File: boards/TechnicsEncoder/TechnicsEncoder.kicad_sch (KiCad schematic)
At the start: 20 parts, among them J1 ISP, J2 Bender, J3 Technics, J4 SelectRX, J5 MIDI In, J6 MIDI Out, J7 BoardCon, J8 PistonEncoder, U1 ATmega48-20P, U2 6N138

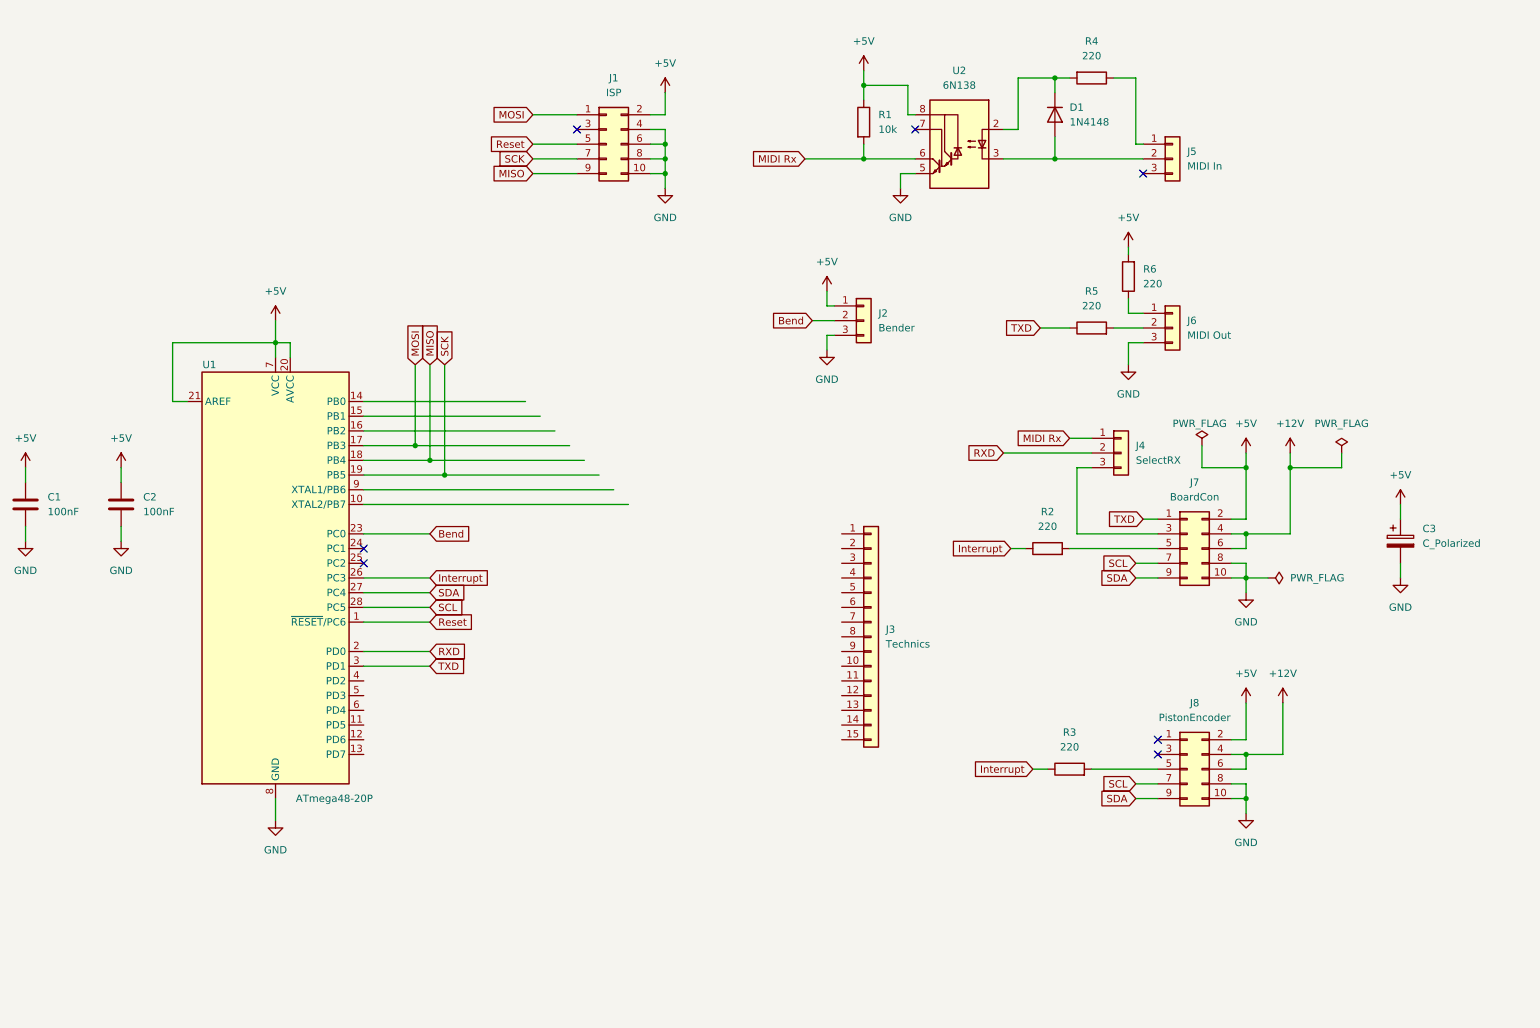
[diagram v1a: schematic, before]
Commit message: Added output buffer to MIDI outputs
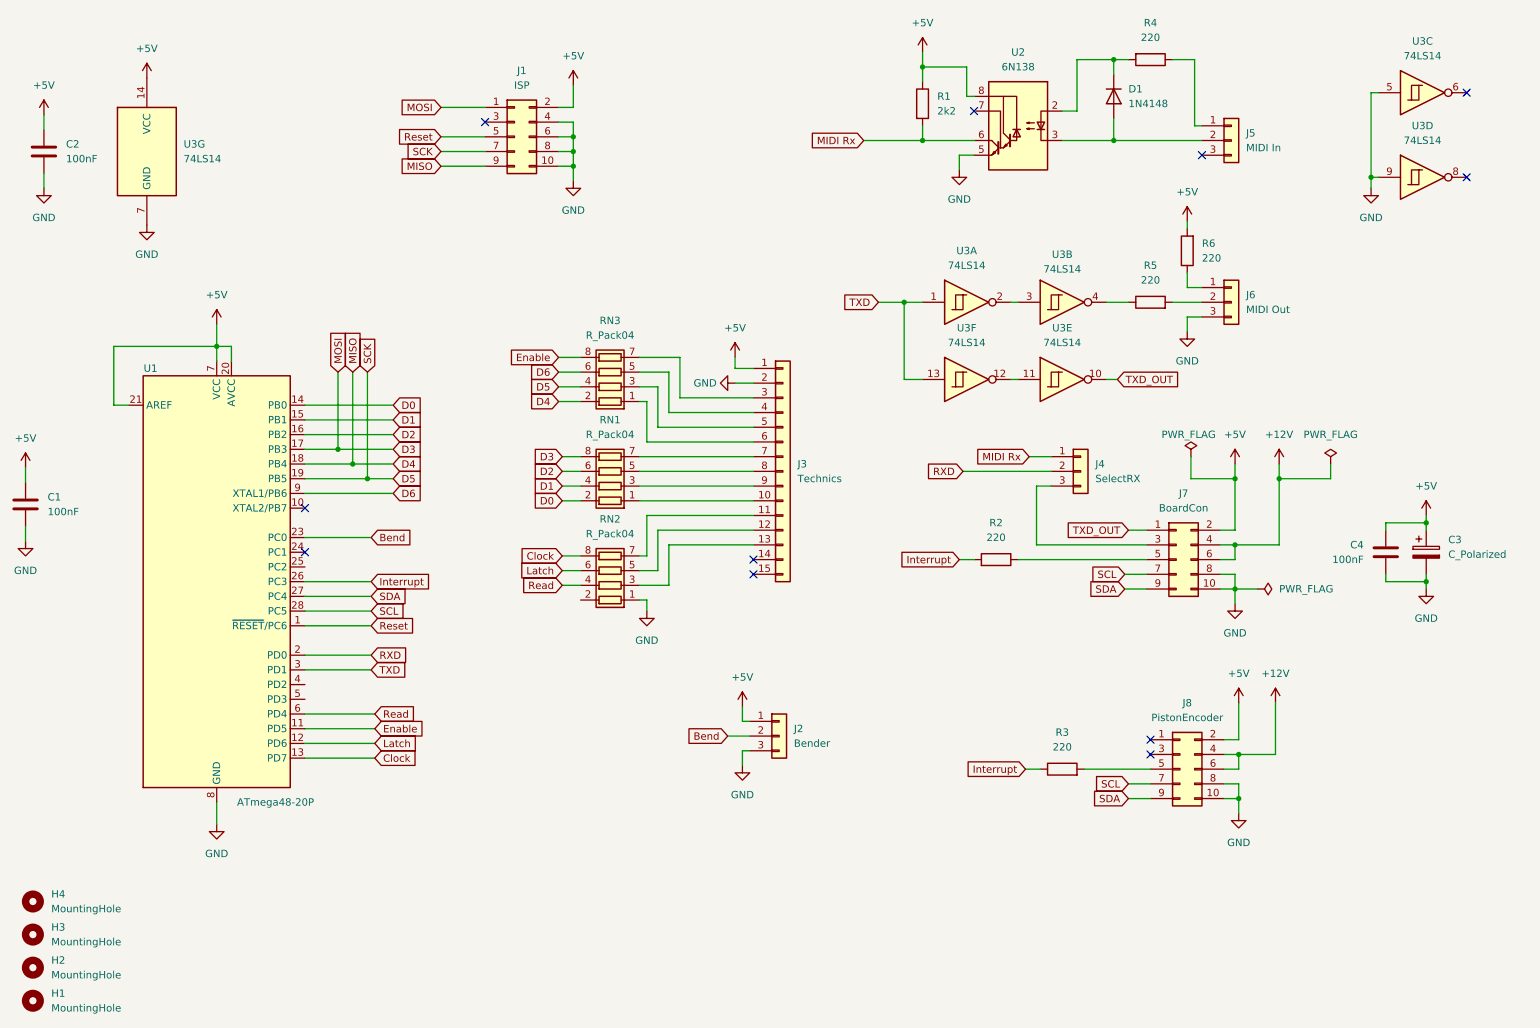
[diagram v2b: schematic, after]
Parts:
- added C4: 100nF, symbol Device:C
- added H1, H2, H3, H4: MountingHole, MountingHole:MountingHole_3mm, symbol Mechanical:MountingHole
- added RN1, RN2, RN3: R_Pack04, symbol Resistors_SIL:R_Pack04_SIL
- added U3: 74LS14, symbol 74xx:74LS14
- R1: value 10k -> 2k2
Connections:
- net +5V: now also J3.1 (Pin_1), C4.1, U3.14 (VCC)
- net GND: now also J3.2 (Pin_2), C4.2, RN2.1 (R1.1), U3.5, U3.7 (GND), U3.9
- net Interrupt: now also R2.2; no longer R2.1
- net TXD: now also U3.1, U3.13; no longer J7.1 (Pin_1), R5.1
- net at J3.10 (Pin_10): now also RN1.1 (R1.1)
- net at J3.11 (Pin_11): now also RN2.7 (R4.1)
- net at J3.12 (Pin_12): now also RN2.5 (R3.1)
- net at J3.13 (Pin_13): now also RN2.3 (R2.1)
- net at J3.3 (Pin_3): now also RN3.7 (R4.1)
- net at J3.4 (Pin_4): now also RN3.5 (R3.1)
- net at J3.5 (Pin_5): now also RN3.3 (R2.1)
- net at J3.6 (Pin_6): now also RN3.1 (R1.1)
- net at J3.7 (Pin_7): now also RN1.7 (R4.1)
- net at J3.8 (Pin_8): now also RN1.5 (R3.1)
- net at J3.9 (Pin_9): now also RN1.3 (R2.1)
- net at J7.5 (Pin_5): now also R2.1; no longer R2.2
- net Enable: now reaches U1.11 (PD5)
- net Enable: now also RN3.8 (R4.2)
- net Latch: now reaches U1.12 (PD6)
- net Latch: now also RN2.6 (R3.2)
- net Clock: now reaches U1.13 (PD7)
- net Clock: now also RN2.8 (R4.2)
- net D0: now reaches U1.14 (PB0)
- net D0: now also RN1.2 (R1.2)
- net D1: now reaches U1.15 (PB1)
- net D1: now also RN1.4 (R2.2)
- net D2: now reaches U1.16 (PB2)
- net D2: now also RN1.6 (R3.2)
- net Read: now reaches U1.6 (PD4)
- net Read: now also RN2.4 (R2.2)
- net D6: now reaches U1.9 (XTAL1/PB6)
- net D6: now also RN3.6 (R3.2)
- net MISO renamed D4
- net D4: now also RN3.2 (R1.2)
- net MOSI renamed D3
- net D3: now also RN1.8 (R4.2)
- net SCK renamed D5
- net D5: now also RN3.4 (R2.2)
- new net: U3.2, U3.3
- new net: R5.1, U3.4
- new net: U3.11, U3.12
- new net TXD_OUT: J7.1 (Pin_1), U3.10
- no-connect marks 7 -> 11
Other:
- moved on the sheet: C2, C3, D1, J1, J2, J3, J4, J5, J6, J7, J8, R1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

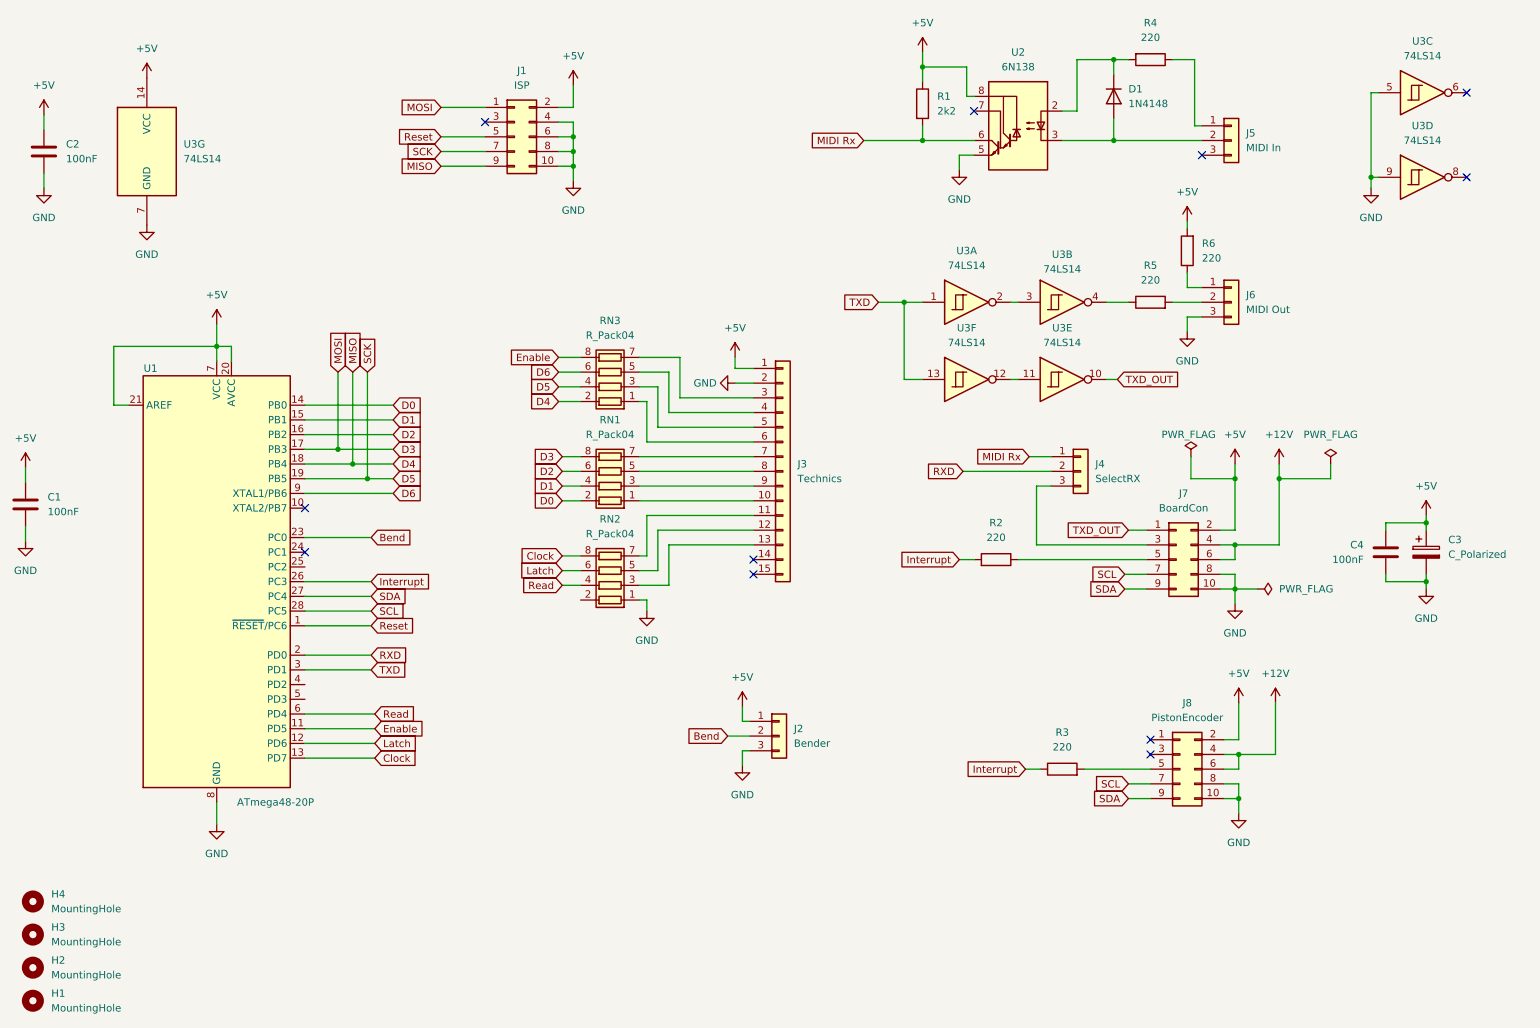
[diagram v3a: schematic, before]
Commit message: Using custom TO220 cooler, fixed and finished several PCBs
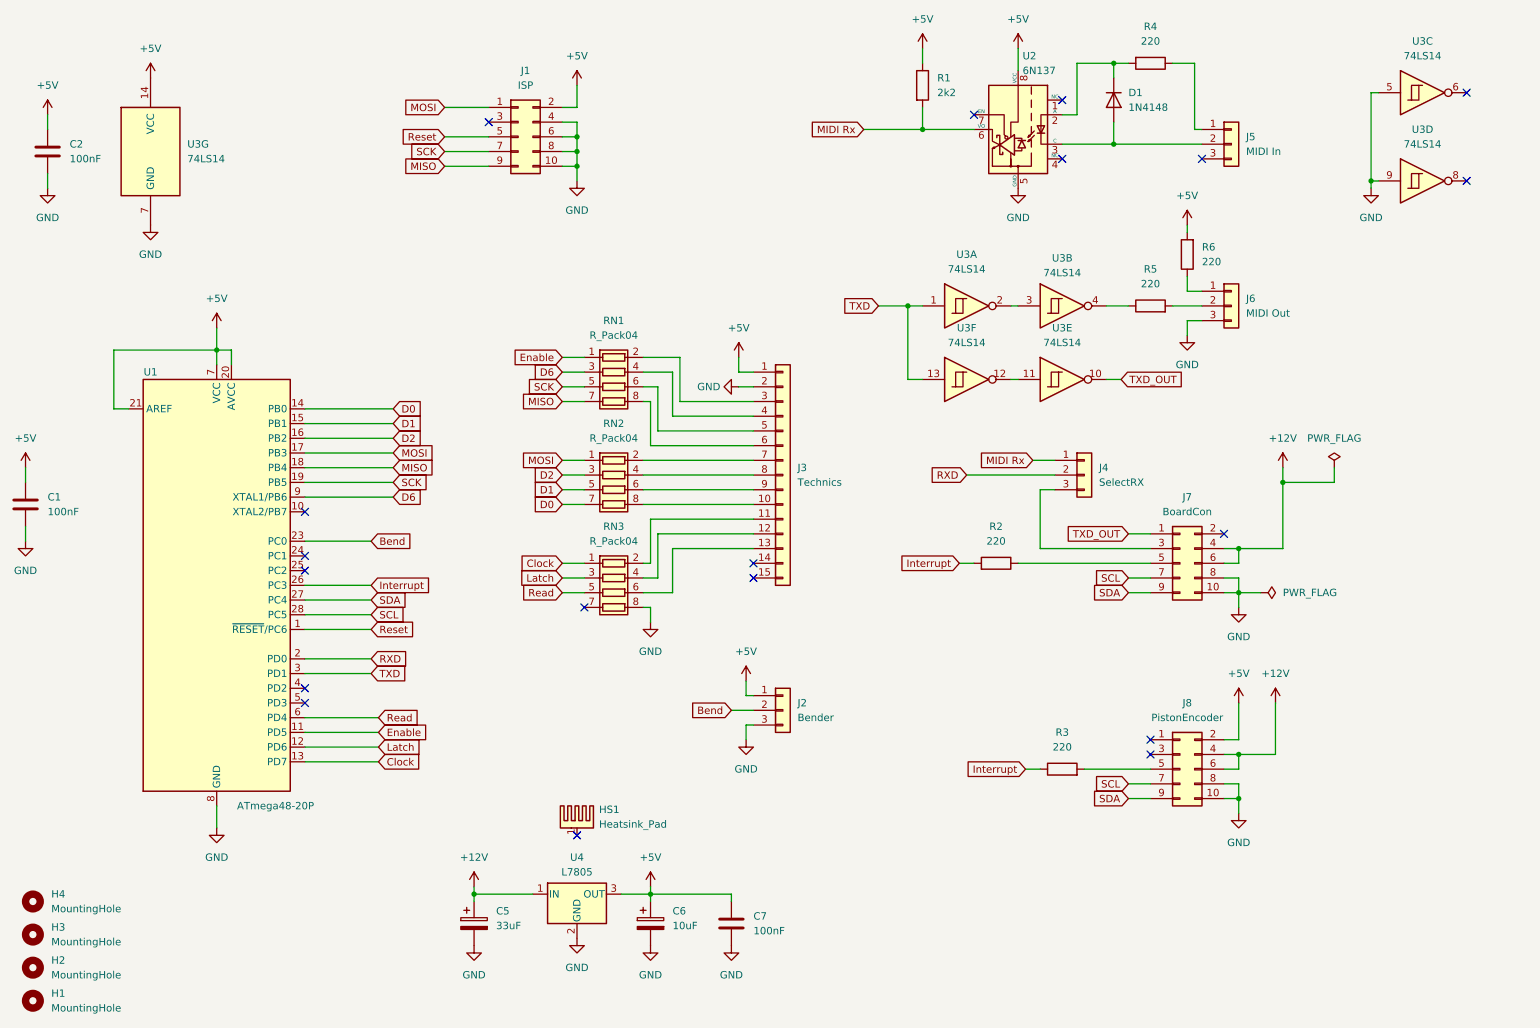
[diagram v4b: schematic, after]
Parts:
- removed C3: C_Polarized, symbol Device:C_Polarized
- removed C4: 100nF, symbol Device:C
- removed RN1, RN2, RN3: R_Pack04, symbol Resistors_SIL:R_Pack04_SIL
- removed U2: 6N138, Package_DIP:DIP-8_W7.62mm, symbol Isolator:6N138
- added C5: 33uF, Capacitor_THT:CP_Radial_D7.5mm_P2.50mm, symbol Device:C_Polarized
- added C6: 10uF, Capacitor_THT:CP_Radial_D6.3mm_P2.50mm, symbol Device:C_Polarized
- added C7: 100nF, Capacitor_THT:C_Disc_D4.3mm_W1.9mm_P5.00mm, symbol Device:C
- added HS1: Heatsink_Pad, Custom_Heatsinks:Heatsink_Aavid_TO-220_H12.7mm, symbol Mechanical:Heatsink_Pad
- added RN1, RN2, RN3: R_Pack04, Resistor_THT:R_Array_SIP8, symbol Custom_Symbols:R_Pack04_SIL
- added U2: 6N137, Package_DIP:DIP-8_W7.62mm, symbol Isolator:6N137
- added U4: L7805, Package_TO_SOT_THT:TO-220-3_Vertical, symbol Regulator_Linear:L7805
- C1, C2: footprint (none) -> Capacitor_THT:C_Disc_D4.3mm_W1.9mm_P5.00mm
- J2, J4, J5, J6: footprint (none) -> Connector_PinHeader_2.54mm:PinHeader_1x03_P2.54mm_Vertical
- J3: footprint (none) -> Connector_JST:JST_PH_B15B-PH-K_1x15_P2.00mm_Vertical
- R2, R3, R5: footprint Resistor_THT:R_Axial_DIN0204_L3.6mm_D1.6mm_P2.54mm_Vertical -> Resistor_THT:R_Axial_DIN0204_L3.6mm_D1.6mm_P7.62mm_Horizontal
- U3: footprint (none) -> Package_DIP:DIP-14_W7.62mm
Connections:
- net +12V: now also C5.1, U4.1 (IN)
- net +5V: now also C6.1, C7.1, U2.8 (VCC), U4.3 (OUT); no longer J7.2 (Pin_2)
- net Clock: now also RN3.1 (R1.1)
- net D0: now also RN2.7 (R4.1)
- net D1: now also RN2.5 (R3.1)
- net D2: now also RN2.3 (R2.1)
- net D6: now also RN1.3 (R2.1)
- net Enable: now also RN1.1 (R1.1)
- net GND: now also C5.2, C6.2, C7.2, RN3.8 (R4.2), U2.5 (GND), U4.2 (GND)
- net Latch: now also RN3.3 (R2.1)
- net MIDI Rx: now also U2.6 (VO)
- net Read: now also RN3.5 (R3.1)
- net at J3.6 (Pin_6): now also RN1.8 (R4.2)
- net at J3.5 (Pin_5): now also RN1.6 (R3.2)
- net at J3.4 (Pin_4): now also RN1.4 (R2.2)
- net at J3.3 (Pin_3): now also RN1.2 (R1.2)
- net at D1.2 (A), J5.2 (Pin_2): now also U2.3 (C)
- net at J3.10 (Pin_10): now also RN2.8 (R4.2)
- net at J3.11 (Pin_11): now also RN3.2 (R1.2)
- net at J3.12 (Pin_12): now also RN3.4 (R2.2)
- net at J3.13 (Pin_13): now also RN3.6 (R3.2)
- net at J3.7 (Pin_7): now also RN2.2 (R1.2)
- net at J3.8 (Pin_8): now also RN2.4 (R2.2)
- net at J3.9 (Pin_9): now also RN2.6 (R3.2)
- net at D1.1 (K), R4.2: now also U2.2 (A)
- net D3 renamed MOSI
- net MOSI: now also RN2.1 (R1.1)
- net D4 renamed MISO
- net MISO: now also RN1.7 (R4.1)
- net D5 renamed SCK
- net SCK: now also RN1.5 (R3.1)
- no-connect marks 11 -> 19
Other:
- moved on the sheet: C2, D1, J1, J2, J3, J4, J5, J6, J7, R1, R2, R4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

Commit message: Added Optocoupler and RS232 converter to UART board lines.
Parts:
- added R7: 220, Resistor_THT:R_Axial_DIN0204_L3.6mm_D1.6mm_P7.62mm_Horizontal, symbol Device:R
- U1: footprint Package_DIP:DIP-28_W7.62mm -> Package_DIP:DIP-28_W7.62mm_Socket
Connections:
- net TXD_OUT: now also R7.2; no longer U3.10
- new net: R7.1, U3.10
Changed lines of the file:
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@@
 	(wire
 		(pts
-			(xy 213.36 80.01) (xy 210.82 80.01)
+			(xy 210.82 80.01) (xy 214.63 80.01)
 		)
 		(stroke
@@
 	(wire
 		(pts
+			(xy 222.25 80.01) (xy 229.87 80.01)
+		)
+		(stroke
+			(width 0)
+			(type default)
+		)
+	)
+	(wire
+		(pts
 			(xy 132.08 104.14) (xy 149.86 104.14)
 		)
@@
 	(global_label "TXD_OUT"
 		(shape input)
-		(at 213.36 80.01 0)
+		(at 229.87 80.01 0)
 		(fields_autoplaced yes)
 		(effects
@@
 		)
 		(property "Intersheetrefs" "${INTERSHEET_REFS}"
-			(at 224.3885 80.01 0)
+			(at 240.8985 80.01 0)
 			(effects
 				(font
@@
 	)
 	(symbol
+		(lib_id "Device:R")
+		(at 218.44 80.01 90)
+		(unit 1)
+		(exclude_from_sim no)
+		(in_bom yes)
+		(on_board yes)
+		(dnp no)
+		(fields_autoplaced yes)
+		(property "Reference" "R7"
+			(at 218.44 73.66 90)
+			(effects
+				(font
+					(size 1.27 1.27)
+				)
+			)
+		)
+		(property "Value" "220"
+			(at 218.44 76.2 90)
+			(effects
+				(font
+					(size 1.27 1.27)
+				)
+			)
+		)
+		(property "Footprint" "Resistor_THT:R_Axial_DIN0204_L3.6mm_D1.6mm_P7.62mm_Horizontal"
+			(at 218.44 81.788 90)
+			(effects
+				(font
+					(size 1.27 1.27)
+				)
+				(hide yes)
+			)
+		)
+		(property "Datasheet" "~"
+			(at 218.44 80.01 0)
+			(effects
+				(font
+					(size 1.27 1.27)
+				)
+				(hide yes)
+			)
+		)
+		(property "Description" "Resistor"
+			(at 218.44 80.01 0)
+			(effects
+				(font
+					(size 1.27 1.27)
+				)
+				(hide yes)
+			)
+		)
+		(pin "1"
+		)
+		(pin "2"
+		)
+		(instances
+			(project "TechnicsEncoder"
+				(path "/bada7ee2-3b4f-486d-8871-f40e51bae2c2"
+					(reference "R7")
+					(unit 1)
+				)
+			)
+		)
+	)
+	(symbol
 		(lib_id "power:+5V")
 		(at 148.59 132.08 0)
@@
 			)
 		)
-		(property "Footprint" "Package_DIP:DIP-28_W7.62mm"
+		(property "Footprint" "Package_DIP:DIP-28_W7.62mm_Socket"
 			(at 57.15 115.57 0)
 			(effects
